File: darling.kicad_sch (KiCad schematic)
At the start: 18 parts, among them J1 USB_C_Receptacle_USB2.0, J2 Conn_01x05, U1 FT230XQ

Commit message: update pictures
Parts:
- J2: footprint Connector_PinHeader_2.54mm:PinHeader_1x05_P2.54mm_Vertical -> Connector_PinHeader_2.54mm:PinHeader_1x05_P2.54mm_Horizontal
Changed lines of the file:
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@@
       (effects (font (size 1.27 1.27)) (justify left))
     )
-    (property "Footprint" "Connector_PinHeader_2.54mm:PinHeader_1x05_P2.54mm_Vertical" (at 156.21 109.22 0)
+    (property "Footprint" "Connector_PinHeader_2.54mm:PinHeader_1x05_P2.54mm_Horizontal" (at 156.21 109.22 0)
       (effects (font (size 1.27 1.27)) hide)
     )

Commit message: minimal touches
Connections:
- net +5V renamed VCC
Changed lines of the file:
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@@
-    (stroke (width 0) (type default))
-  )
-  (wire (pts (xy 105.41 72.39) (xy 106.68 72.39))
     (stroke (width 0) (type default))
   )
@@
     (stroke (width 0) (type default))
   )
+  (label "RTS" (at 146.05 77.47 0) (fields_autoplaced)
+    (effects (font (size 1.27 1.27)) (justify left bottom))
+  )
+  (label "TX" (at 149.86 111.76 180) (fields_autoplaced)
+    (effects (font (size 1.27 1.27)) (justify right bottom))
+  )
+  (label "RX" (at 146.05 74.93 0) (fields_autoplaced)
+    (effects (font (size 1.27 1.27)) (justify left bottom))
+  )
+  (label "CTS" (at 146.05 80.01 0) (fields_autoplaced)
+    (effects (font (size 1.27 1.27)) (justify left bottom))
+  )
+  (label "RX" (at 149.86 109.22 180) (fields_autoplaced)
+    (effects (font (size 1.27 1.27)) (justify right bottom))
+  )
   (label "RXLED" (at 146.05 87.63 0) (fields_autoplaced)
     (effects (font (size 1.27 1.27)) (justify left bottom))
   )
+  (label "TX" (at 146.05 72.39 0) (fields_autoplaced)
+    (effects (font (size 1.27 1.27)) (justify left bottom))
+  )
   (label "TXLED" (at 146.05 90.17 0) (fields_autoplaced)
     (effects (font (size 1.27 1.27)) (justify left bottom))
-  )
-  (global_label "RTS" (shape input) (at 146.05 77.47 0)
-    (effects (font (size 1.27 1.27)) (justify left))
-    (property "Intersheetrefs" "${INTERSHEET_REFS}" (at 146.05 77.47 0)
-      (effects (font (size 1.27 1.27)) hide)
-    )
-  )
-  (global_label "TX" (shape input) (at 149.86 111.76 180)
-    (effects (font (size 1.27 1.27)) (justify right))
-    (property "Intersheetrefs" "${INTERSHEET_REFS}" (at 149.86 111.76 0)
-      (effects (font (size 1.27 1.27)) hide)
-    )
-  )
-  (global_label "CTS" (shape input) (at 146.05 80.01 0)
-    (effects (font (size 1.27 1.27)) (justify left))
-    (property "Intersheetrefs" "${INTERSHEET_REFS}" (at 146.05 80.01 0)
-      (effects (font (size 1.27 1.27)) hide)
-    )
-  )
-  (global_label "RX" (shape input) (at 146.05 74.93 0)
-    (effects (font (size 1.27 1.27)) (justify left))
-    (property "Intersheetrefs" "${INTERSHEET_REFS}" (at 146.05 74.93 0)
-      (effects (font (size 1.27 1.27)) hide)
-    )
-  )
-  (global_label "VCCIO" (shape input) (at 105.41 72.39 180)
-    (effects (font (size 1.27 1.27)) (justify right))
-    (property "Intersheetrefs" "${INTERSHEET_REFS}" (at 105.41 72.39 0)
-      (effects (font (size 1.27 1.27)) hide)
-    )
-  )
-  (global_label "VCCIO" (shape input) (at 129.54 62.23 90)
-    (effects (font (size 1.27 1.27)) (justify left))
-    (property "Intersheetrefs" "${INTERSHEET_REFS}" (at 129.54 62.23 0)
-      (effects (font (size 1.27 1.27)) hide)
-    )
-  )
-  (global_label "TX" (shape input) (at 146.05 72.39 0)
-    (effects (font (size 1.27 1.27)) (justify left))
-    (property "Intersheetrefs" "${INTERSHEET_REFS}" (at 146.05 72.39 0)
-      (effects (font (size 1.27 1.27)) hide)
-    )
-  )
-  (global_label "RX" (shape input) (at 149.86 109.22 180)
-    (effects (font (size 1.27 1.27)) (justify right))
-    (property "Intersheetrefs" "${INTERSHEET_REFS}" (at 149.86 109.22 0)
-      (effects (font (size 1.27 1.27)) hide)
-    )
   )
   (symbol (lib_id "Interface_USB:FT230XQ") (at 127 82.55 0) (unit 1)
@@
     )
   )
-  (symbol (lib_id "power:+5V") (at 149.86 102.87 0) (unit 1)
-    (in_bom yes) (on_board yes) (dnp no)
-    (property "Reference" "#PWR03" (at 149.86 106.68 0)
-      (effects (font (size 1.27 1.27)) hide)
-    )
-    (property "Value" "+5V" (at 149.86 99.06 0)
+  (symbol (lib_id "Device:C_Small") (at 85.09 67.31 0) (unit 1)
+    (in_bom yes) (on_board yes) (dnp no)
+    (property "Reference" "C1" (at 88.011 66.1416 0)
+      (effects (font (size 1.27 1.27)) (justify left))
+    )
+    (property "Value" "10nF" (at 88.011 68.453 0)
+      (effects (font (size 1.27 1.27)) (justify left))
+    )
+    (property "Footprint" "Capacitor_SMD:C_0402_1005Metric" (at 85.09 67.31 0)
+      (effects (font (size 1.27 1.27)) hide)
+    )
+    (property "Datasheet" "~" (at 85.09 67.31 0)
+      (effects (font (size 1.27 1.27)) hide)
+    )
+    (pin "1")
+    (pin "2")
+    (instances
+      (project "darling"
+        (path "/e59a511f-97b2-46f0-a377-a631c632cd45"
+          (reference "C1") (unit 1)
+        )
+      )
+    )
+  )
+  (symbol (lib_id "power:+3V3") (at 129.54 62.23 0) (unit 1)
+    (in_bom yes) (on_board yes) (dnp no)
+    (property "Reference" "#PWR03" (at 129.54 66.04 0)
+      (effects (font (size 1.27 1.27)) hide)
+    )
+    (property "Value" "+3V3" (at 129.54 58.42 0)
+      (effects (font (size 1.27 1.27)))
+    )
+    (property "Footprint" "" (at 129.54 62.23 0)
+      (effects (font (size 1.27 1.27)) hide)
+    )
+    (property "Datasheet" "" (at 129.54 62.23 0)
+      (effects (font (size 1.27 1.27)) hide)
+    )
+    (pin "1")
+    (instances
+      (project "darling"
+        (path "/e59a511f-97b2-46f0-a377-a631c632cd45"
+          (reference "#PWR03") (unit 1)
+        )
+      )
+    )
+  )
+  (symbol (lib_id "power:VCC") (at 124.46 62.23 0) (unit 1)
+    (in_bom yes) (on_board yes) (dnp no)
+    (property "Reference" "#PWR05" (at 124.46 66.04 0)
+      (effects (font (size 1.27 1.27)) hide)
+    )
+    (property "Value" "VCC" (at 124.46 58.42 0)
+      (effects (font (size 1.27 1.27)))
+    )
+    (property "Footprint" "" (at 124.46 62.23 0)
+      (effects (font (size 1.27 1.27)) hide)
+    )
+    (property "Datasheet" "" (at 124.46 62.23 0)
+      (effects (font (size 1.27 1.27)) hide)
+    )
+    (pin "1")
+    (instances
+      (project "darling"
+        (path "/e59a511f-97b2-46f0-a377-a631c632cd45"
+          (reference "#PWR05") (unit 1)
+        )
+      )
+    )
+  )
+  (symbol (lib_id "power:VCC") (at 76.2 102.87 0) (unit 1)
+    (in_bom yes) (on_board yes) (dnp no)
+    (property "Reference" "#PWR02" (at 76.2 106.68 0)
+      (effects (font (size 1.27 1.27)) hide)
+    )
+    (property "Value" "VCC" (at 76.2 99.06 0)
+      (effects (font (size 1.27 1.27)))
+    )
+    (property "Footprint" "" (at 76.2 102.87 0)
+      (effects (font (size 1.27 1.27)) hide)
+    )
+    (property "Datasheet" "" (at 76.2 102.87 0)
+      (effects (font (size 1.27 1.27)) hide)
+    )
+    (pin "1")
+    (instances
+      (project "darling"
+        (path "/e59a511f-97b2-46f0-a377-a631c632cd45"
+          (reference "#PWR02") (unit 1)
+        )
+      )
+    )
+  )
+  (symbol (lib_id "power:VCC") (at 149.86 102.87 0) (unit 1)
+    (in_bom yes) (on_board yes) (dnp no)
+    (property "Reference" "#PWR01" (at 149.86 106.68 0)
+      (effects (font (size 1.27 1.27)) hide)
+    )
+    (property "Value" "VCC" (at 149.86 99.06 0)
       (effects (font (size 1.27 1.27)))
     )
@@
       (project "darling"
         (path "/e59a511f-97b2-46f0-a377-a631c632cd45"
-          (reference "#PWR03") (unit 1)
-        )
-      )
-    )
-  )
-  (symbol (lib_id "Device:C_Small") (at 85.09 67.31 0) (unit 1)
-    (in_bom yes) (on_board yes) (dnp no)
-    (property "Reference" "C1" (at 88.011 66.1416 0)
-      (effects (font (size 1.27 1.27)) (justify left))
-    )
-    (property "Value" "10nF" (at 88.011 68.453 0)
-      (effects (font (size 1.27 1.27)) (justify left))
-    )
-    (property "Footprint" "Capacitor_SMD:C_0402_1005Metric" (at 85.09 67.31 0)
-      (effects (font (size 1.27 1.27)) hide)
-    )
-    (property "Datasheet" "~" (at 85.09 67.31 0)
-      (effects (font (size 1.27 1.27)) hide)
-    )
-    (pin "1")
-    (pin "2")
-    (instances
-      (project "darling"
-        (path "/e59a511f-97b2-46f0-a377-a631c632cd45"
-          (reference "C1") (unit 1)
+          (reference "#PWR01") (unit 1)
         )
       )
@@
     )
   )
-  (symbol (lib_id "power:+5V") (at 76.2 102.87 0) (unit 1)
-    (in_bom yes) (on_board yes) (dnp no)
-    (property "Reference" "#PWR01" (at 76.2 106.68 0)
-      (effects (font (size 1.27 1.27)) hide)
-    )
-    (property "Value" "+5V" (at 76.2 99.06 0)
-      (effects (font (size 1.27 1.27)))
-    )
-    (property "Footprint" "" (at 76.2 102.87 0)
-      (effects (font (size 1.27 1.27)) hide)
-    )
-    (property "Datasheet" "" (at 76.2 102.87 0)
-      (effects (font (size 1.27 1.27)) hide)
-    )
-    (pin "1")
-    (instances
-      (project "darling"
-        (path "/e59a511f-97b2-46f0-a377-a631c632cd45"
-          (reference "#PWR01") (unit 1)
-        )
-      )
-    )
-  )
   (symbol (lib_id "power:+3V3") (at 144.78 102.87 0) (unit 1)
     (in_bom yes) (on_board yes) (dnp no)
@@
         )
       )
-    )
-  )
-  (symbol (lib_id "power:+5V") (at 124.46 62.23 0) (unit 1)
-    (in_bom yes) (on_board yes) (dnp no)
-    (property "Reference" "#PWR02" (at 124.46 66.04 0)
-      (effects (font (size 1.27 1.27)) hide)
-    )
-    (property "Value" "+5V" (at 124.46 58.42 0)
-      (effects (font (size 1.27 1.27)))
-    )
-    (property "Footprint" "" (at 124.46 62.23 0)
-      (effects (font (size 1.27 1.27)) hide)
-    )
-    (property "Datasheet" "" (at 124.46 62.23 0)
-      (effects (font (size 1.27 1.27)) hide)
-    )
-    (pin "1")
-    (instances
-      (project "darling"
-        (path "/e59a511f-97b2-46f0-a377-a631c632cd45"
-          (reference "#PWR02") (unit 1)
-        )
-      )

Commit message: final rev 4
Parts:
- added TP1, TP2: TestPoint, TestPoint:TestPoint_Pad_D1.0mm, symbol Connector:TestPoint
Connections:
- net CTS: now also TP2.1
- net RTS: now also TP1.1
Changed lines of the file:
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@@
+    (effects (font (size 1.27 1.27)) (justify right bottom))
+  )
+  (label "RTS" (at 115.57 116.84 180) (fields_autoplaced)
     (effects (font (size 1.27 1.27)) (justify right bottom))
   )
@@
   (label "RXLED" (at 146.05 87.63 0) (fields_autoplaced)
     (effects (font (size 1.27 1.27)) (justify left bottom))
+  )
+  (label "CTS" (at 115.57 121.92 180) (fields_autoplaced)
+    (effects (font (size 1.27 1.27)) (justify right bottom))
   )
   (label "TX" (at 146.05 72.39 0) (fields_autoplaced)
@@
     )
   )
+  (symbol (lib_id "Connector:TestPoint") (at 115.57 116.84 270) (unit 1)
+    (in_bom yes) (on_board yes) (dnp no) (fields_autoplaced)
+    (property "Reference" "TP1" (at 120.65 115.57 90)
+      (effects (font (size 1.27 1.27)) (justify left))
+    )
+    (property "Value" "TestPoint" (at 120.65 118.11 90)
+      (effects (font (size 1.27 1.27)) (justify left))
+    )
+    (property "Footprint" "TestPoint:TestPoint_Pad_D1.0mm" (at 115.57 121.92 0)
+      (effects (font (size 1.27 1.27)) hide)
+    )
+    (property "Datasheet" "~" (at 115.57 121.92 0)
+      (effects (font (size 1.27 1.27)) hide)
+    )
+    (pin "1")
+    (instances
+      (project "darling"
+        (path "/e59a511f-97b2-46f0-a377-a631c632cd45"
+          (reference "TP1") (unit 1)
+        )
+      )
+    )
+  )
   (symbol (lib_id "power:+3V3") (at 106.68 71.12 0) (unit 1)
     (in_bom yes) (on_board yes) (dnp no)
@@
         )
       )
+    )
+  )
+  (symbol (lib_id "Connector:TestPoint") (at 115.57 121.92 270) (unit 1)
+    (in_bom yes) (on_board yes) (dnp no) (fields_autoplaced)
+    (property "Reference" "TP2" (at 120.65 120.65 90)
+      (effects (font (size 1.27 1.27)) (justify left))
+    )
+    (property "Value" "TestPoint" (at 120.65 123.19 90)
+      (effects (font (size 1.27 1.27)) (justify left))
+    )
+    (property "Footprint" "TestPoint:TestPoint_Pad_D1.0mm" (at 115.57 127 0)
+      (effects (font (size 1.27 1.27)) hide)
+    )
+    (property "Datasheet" "~" (at 115.57 127 0)
+      (effects (font (size 1.27 1.27)) hide)
+    )
+    (pin "1")
+    (instances
+      (project "darling"
+        (path "/e59a511f-97b2-46f0-a377-a631c632cd45"
+          (reference "TP2") (unit 1)
+        )
+      )

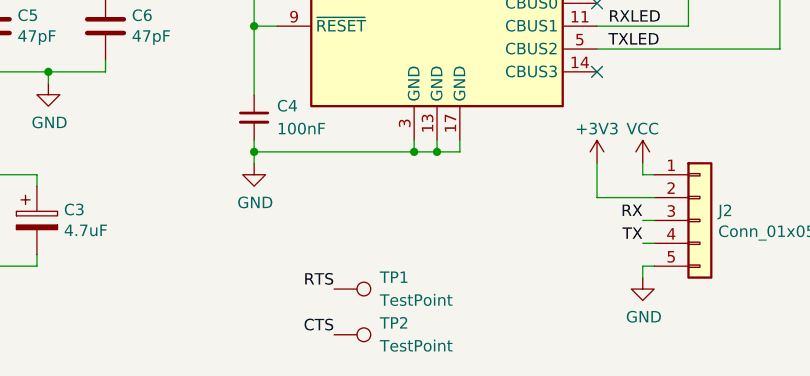
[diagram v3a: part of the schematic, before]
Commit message: update readme and images
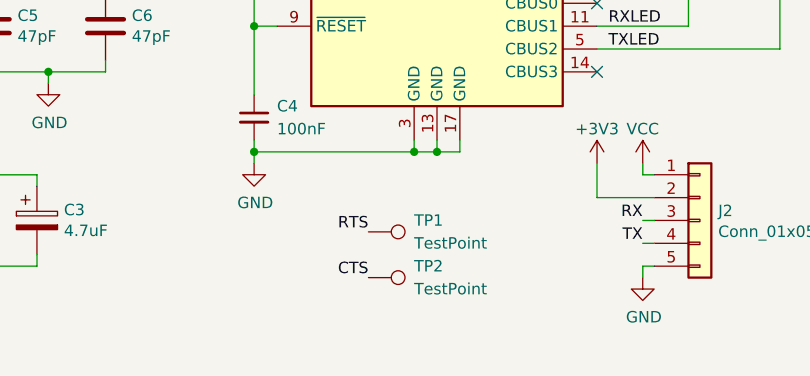
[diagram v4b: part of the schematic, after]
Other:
- moved on the sheet: TP1, TP2
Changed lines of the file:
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@@
     (effects (font (size 1.27 1.27)) (justify right bottom))
   )
-  (label "RTS" (at 115.57 116.84 180) (fields_autoplaced)
+  (label "RTS" (at 119.38 110.49 180) (fields_autoplaced)
     (effects (font (size 1.27 1.27)) (justify right bottom))
   )
@@
     (effects (font (size 1.27 1.27)) (justify left bottom))
   )
-  (label "CTS" (at 115.57 121.92 180) (fields_autoplaced)
+  (label "CTS" (at 119.38 115.57 180) (fields_autoplaced)
     (effects (font (size 1.27 1.27)) (justify right bottom))
   )
@@
     )
   )
-  (symbol (lib_id "Connector:TestPoint") (at 115.57 116.84 270) (unit 1)
+  (symbol (lib_id "Connector:TestPoint") (at 119.38 110.49 270) (unit 1)
     (in_bom yes) (on_board yes) (dnp no) (fields_autoplaced)
-    (property "Reference" "TP1" (at 120.65 115.57 90)
-      (effects (font (size 1.27 1.27)) (justify left))
-    )
-    (property "Value" "TestPoint" (at 120.65 118.11 90)
-      (effects (font (size 1.27 1.27)) (justify left))
-    )
-    (property "Footprint" "TestPoint:TestPoint_Pad_D1.0mm" (at 115.57 121.92 0)
-      (effects (font (size 1.27 1.27)) hide)
-    )
-    (property "Datasheet" "~" (at 115.57 121.92 0)
+    (property "Reference" "TP1" (at 124.46 109.22 90)
+      (effects (font (size 1.27 1.27)) (justify left))
+    )
+    (property "Value" "TestPoint" (at 124.46 111.76 90)
+      (effects (font (size 1.27 1.27)) (justify left))
+    )
+    (property "Footprint" "TestPoint:TestPoint_Pad_D1.0mm" (at 119.38 115.57 0)
+      (effects (font (size 1.27 1.27)) hide)
+    )
+    (property "Datasheet" "~" (at 119.38 115.57 0)
       (effects (font (size 1.27 1.27)) hide)
     )
@@
     )
   )
-  (symbol (lib_id "Connector:TestPoint") (at 115.57 121.92 270) (unit 1)
+  (symbol (lib_id "Connector:TestPoint") (at 119.38 115.57 270) (unit 1)
     (in_bom yes) (on_board yes) (dnp no) (fields_autoplaced)
-    (property "Reference" "TP2" (at 120.65 120.65 90)
-      (effects (font (size 1.27 1.27)) (justify left))
-    )
-    (property "Value" "TestPoint" (at 120.65 123.19 90)
-      (effects (font (size 1.27 1.27)) (justify left))
-    )
-    (property "Footprint" "TestPoint:TestPoint_Pad_D1.0mm" (at 115.57 127 0)
-      (effects (font (size 1.27 1.27)) hide)
-    )
-    (property "Datasheet" "~" (at 115.57 127 0)
-      (effects (font (size 1.27 1.27)) hide)
-    )
+    (property "Reference" "TP2" (at 124.46 114.3 90)
+      (effects (font (size 1.27 1.27)) (justify left))
+    )
+    (property "Value" "TestPoint" (at 124.46 116.84 90)
+      (effects (font (size 1.27 1.27)) (justify left))
+    )
+    (property "Footprint" "TestPoint:TestPoint_Pad_D1.0mm" (at 119.38 120.65 0)
+      (effects (font (size 1.27 1.27)) hide)
+    )
+    (property "Datasheet" "~" (at 119.38 120.65 0)
+      (effects (font (size 1.27 1.27)) hide)
+    )
